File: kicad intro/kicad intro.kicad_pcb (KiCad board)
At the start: 2 copper layers, 31.8 x 33.8 mm, 14 parts, among them J1 USB_C_Receptacle_PowerOnly_6P, J2 Conn_01x03_Socket, J3 Conn_01x03_Socket, Q1 BF459, U1 ATtiny85-20P

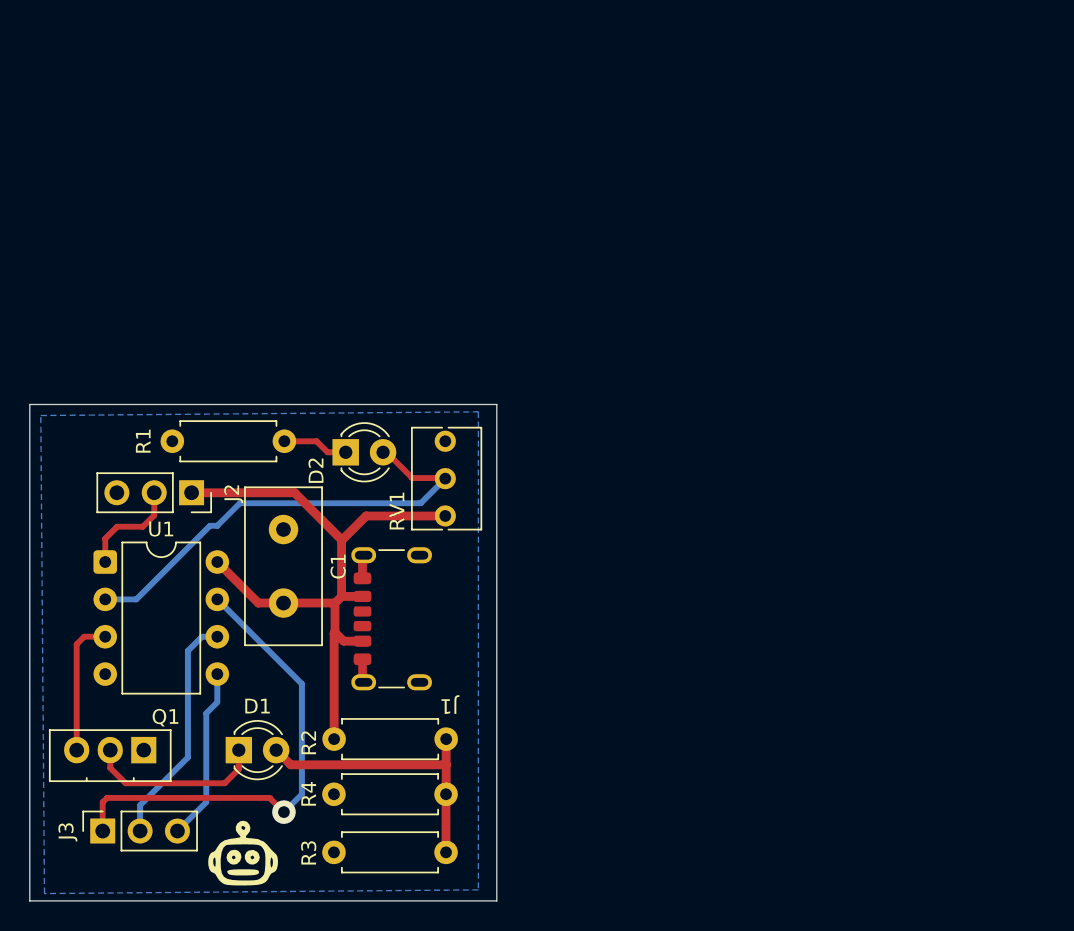
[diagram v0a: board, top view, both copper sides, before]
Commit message: Separated ground pours
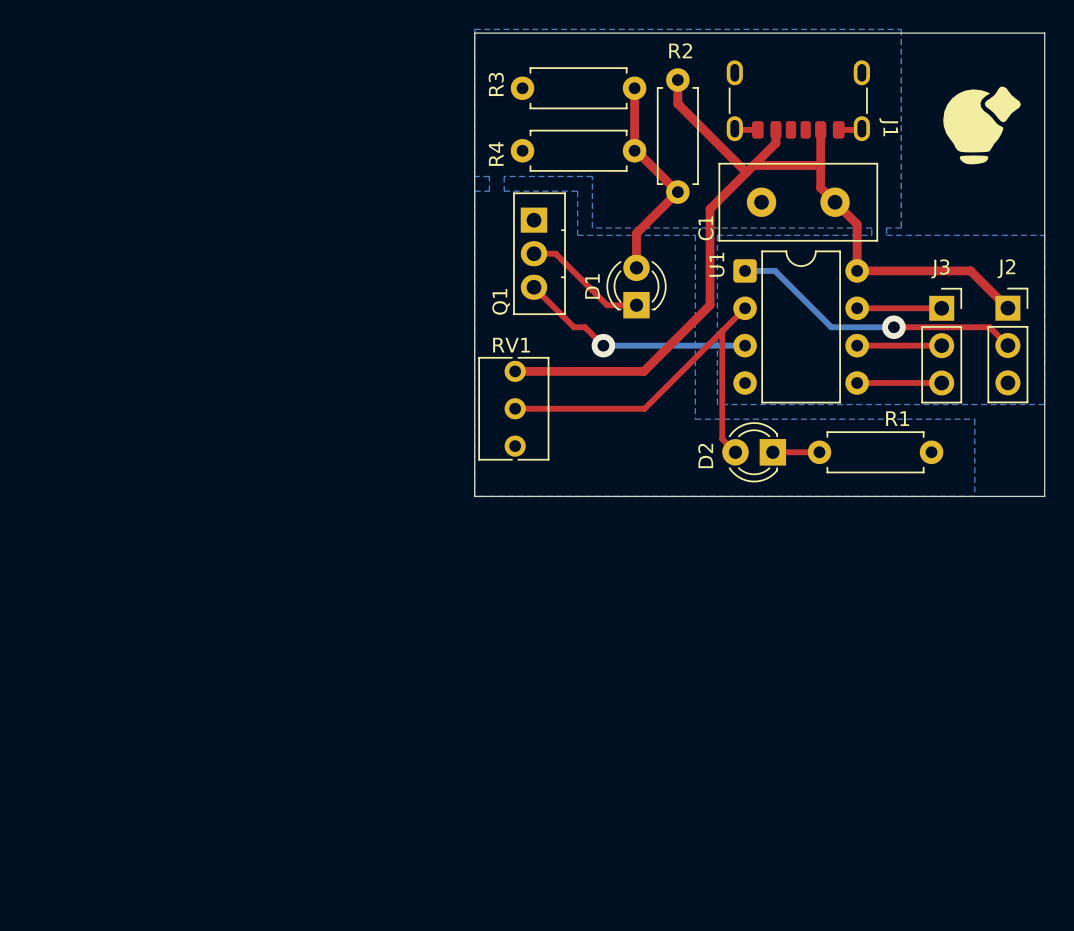
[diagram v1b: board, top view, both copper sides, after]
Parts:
- removed the G*** at (145.2, 108.8)
- added G***: LOGO, icons:logo_bulb, F.Cu at (195.5, 59.2)
- moved J3 67.2 mm to (192.8, 71.7), turned to 0 degrees
- moved J2 56.9 mm to (197.2, 71.7), turned to 0 degrees
- moved R3 53.5 mm to (171.9, 56.8)
- moved R1 51.6 mm to (192.1, 81.5), turned to 180 degrees
- moved R2 50.5 mm to (174.8, 56.2), turned to -90 degrees
- moved U1 47.8 mm to (179.4, 69.2)
- moved R4 45.6 mm to (171.9, 61.0)
- moved J1 45.0 mm to (183.0, 56.5), turned to 180 degrees
- moved Q1 44.7 mm to (165.0, 65.7), turned to -90 degrees
- moved D1 40.6 mm to (172.0, 71.5), turned to 90 degrees
- moved C1 39.4 mm to (180.5, 64.5), turned to 0 degrees
- moved D2 29.0 mm to (181.3, 81.5), turned to 180 degrees
- moved RV1 4.76 mm to (163.8, 81.1), turned to -90 degrees
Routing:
- net PB2/SCK/SCL: track 32.2 -> 5.75 mm, vias 1 -> 0
- net +5V: track 45.7 -> 63.6 mm
- net PB5/RESET: track 7.11 -> 20.0 mm, vias 0 -> 1
- net PB1/MISO: track 16.0 -> 5.75 mm
- net Net-(Q1-B): track 9.35 -> 16.0 mm, vias 0 -> 1
- net PB0/MOSI/SDA: track 11.8 -> 5.75 mm
- net +3.3V: track 19.7 -> 14.7 mm
- net Net-(D2-A): track 31.5 -> 27.0 mm
- net Net-(D1-K): track 12.1 -> 8.42 mm
- net Net-(D2-K): track 4.48 -> 3.17 mm
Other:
- board size 31.8 x 33.8 mm -> 38.8 x 31.5 mm
- board text added: "3.1 cm"
- board text added: "3.9 cm"

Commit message: Updated sample code and design
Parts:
- removed D2: LED, LED_THT:LED_D3.0mm
- removed R1: 220, Resistor_THT:R_Axial_DIN0207_L6.3mm_D2.5mm_P7.62mm_Horizontal
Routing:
- net Net-(U1-XTAL1/PB3): track 27.0 -> 18.5 mm
- net Net-(D2-K): track 3.17 -> 0.00 mm
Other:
- board size 38.8 x 31.5 mm -> 38.8 x 30 mm
- board text added: "3 cm"
- board text removed: "3.1 cm"
